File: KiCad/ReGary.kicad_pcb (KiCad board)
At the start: 4 copper layers, 38 x 38 mm, 36 parts, among them U1 10M02SCU169C8G, U2 LM1117-3.3, U3 SN74CBTD16210, U4 SN74CBTD16210, U5 SN74CBTD16210, U6 SN74CBTD16210, U7 PLCC_84_plug, U8 PLCC_84_plug

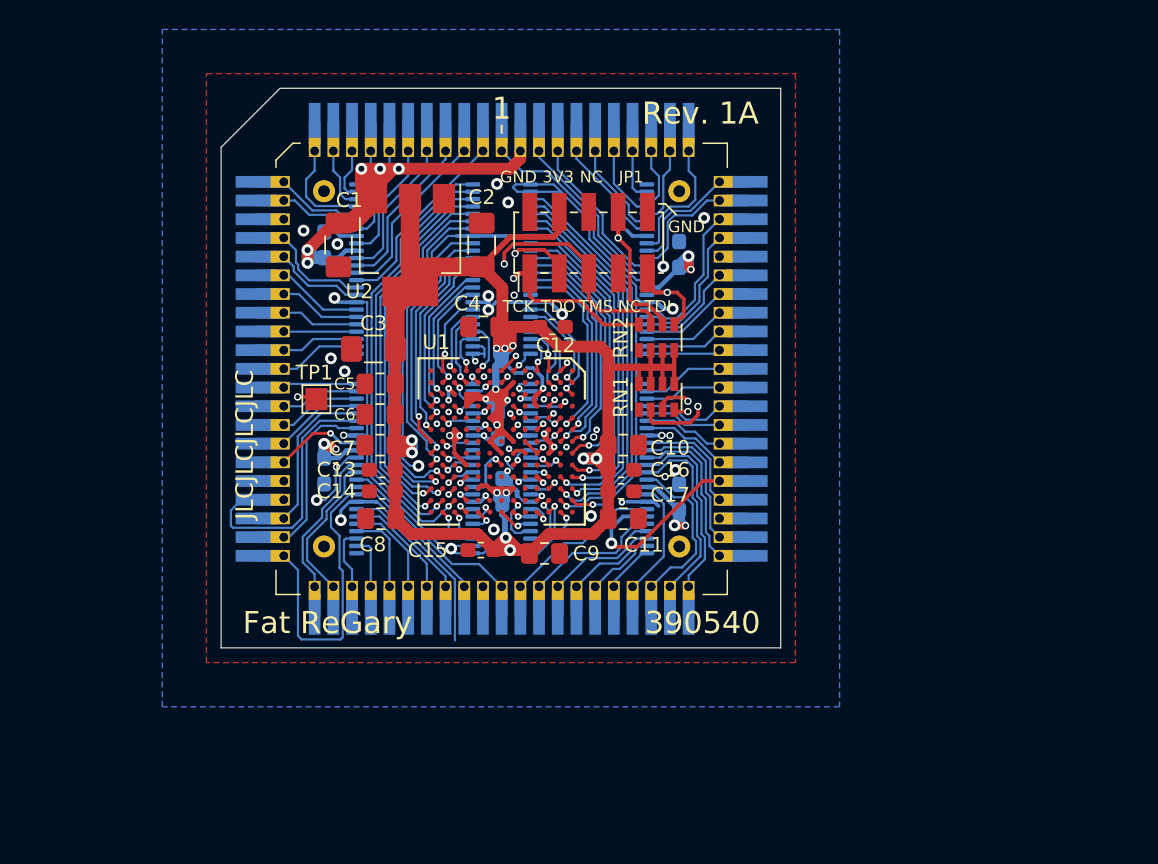
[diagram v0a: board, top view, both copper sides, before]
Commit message: Add Fat Gary socket symbol and change to it
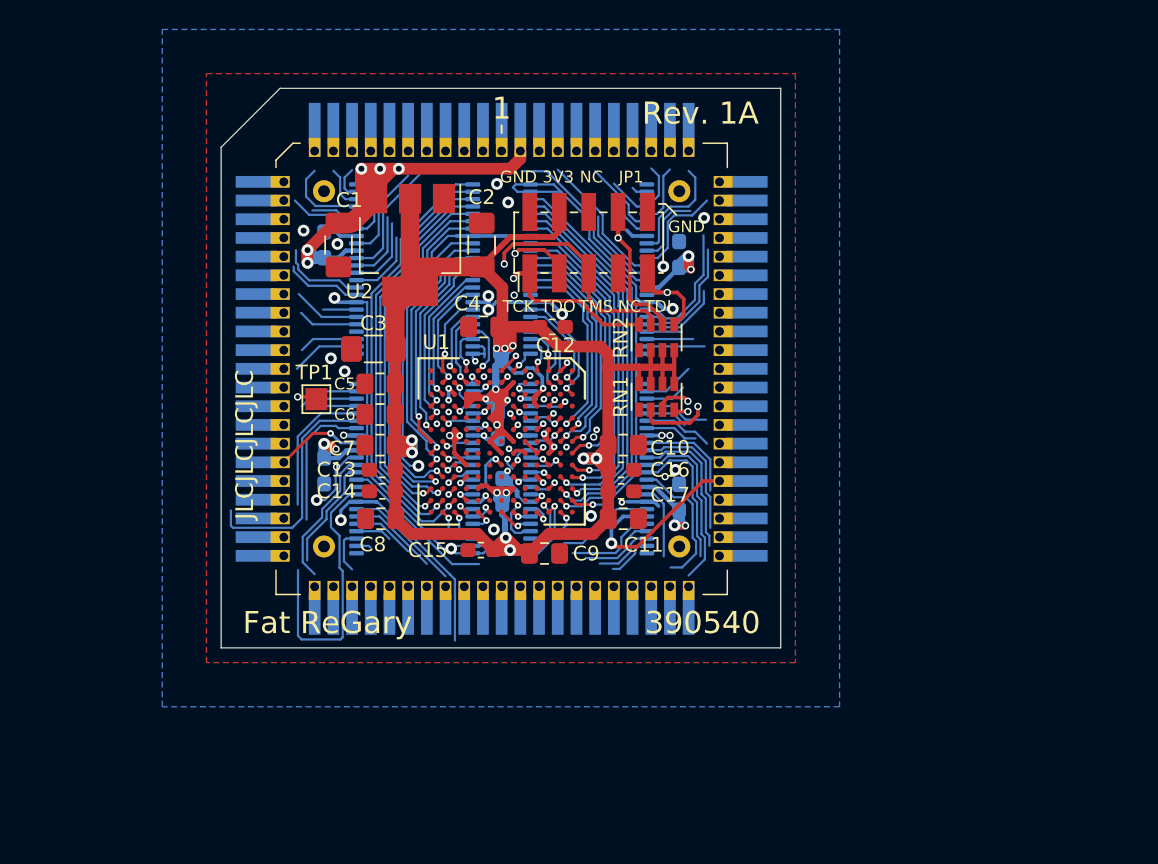
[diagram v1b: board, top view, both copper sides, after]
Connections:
- U7 pad 1: FCS -> Net-(U7-Pad1)
- U7 pad 10: DS -> Net-(U7-Pad10)
- U7 pad 11: DSACK0 -> Net-(U7-Pad11)
- U7 pad 12: DSACK1 -> Net-(U7-Pad12)
- U7 pad 13: STERM -> Net-(U7-Pad13)
- U7 pad 14: GND -> Net-(U7-Pad14)
- U7 pad 15: RMC -> Net-(U7-Pad15)
- U7 pad 16: SBR -> Net-(U7-Pad16)
- U7 pad 17: SBG -> Net-(U7-Pad17)
- U7 pad 18: CIIN -> Net-(U7-Pad18)
- U7 pad 19: MTACK -> Net-(U7-Pad19)
- U7 pad 2: CCS -> Net-(U7-Pad2)
- U7 pad 20: DTACK -> Net-(U7-Pad20)
- U7 pad 21: DOE -> Net-(U7-Pad21)
- U7 pad 22: WAIT -> Net-(U7-Pad22)
- U7 pad 23: BR -> Net-(U7-Pad23)
- U7 pad 24: BG -> Net-(U7-Pad24)
- U7 pad 25: BGACK -> Net-(U7-Pad25)
- U7 pad 26: HLT -> Net-(U7-Pad26)
- U7 pad 27: BERR -> Net-(U7-Pad27)
- U7 pad 28: GND -> Net-(U7-Pad28)
- U7 pad 29: RESET -> Net-(U7-Pad29)
- U7 pad 3: A2 -> Net-(U7-Pad3)
- U7 pad 30: CPUCLK -> Net-(U7-Pad30)
- U7 pad 31: C7M -> Net-(U7-Pad31)
- U7 pad 32: CDAC -> Net-(U7-Pad32)
- U7 pad 33: D2P -> Net-(U7-Pad33)
- U7 pad 34: DBOE1 -> Net-(U7-Pad34)
- U7 pad 35: DBOE0 -> Net-(U7-Pad35)
- U7 pad 36: DBR16 -> Net-(U7-Pad36)
- U7 pad 37: DBLT -> Net-(U7-Pad37)
- U7 pad 38: READ -> Net-(U7-Pad38)
- U7 pad 39: EDS2 -> Net-(U7-Pad39)
- U7 pad 4: A1 -> Net-(U7-Pad4)
- U7 pad 40: EDS3 -> Net-(U7-Pad40)
- U7 pad 41: LOCK_EA1 -> Net-(U7-Pad41)
- U7 pad 42: VCC -> Net-(U7-Pad42)
- U7 pad 43: ABOE2 -> Net-(U7-Pad43)
- U7 pad 44: ABOE0 -> Net-(U7-Pad44)
- U7 pad 45: MS2 -> Net-(U7-Pad45)
- U7 pad 46: MTCR -> Net-(U7-Pad46)
- U7 pad 47: CINH -> Net-(U7-Pad47)
- U7 pad 48: A3 -> Net-(U7-Pad48)
- U7 pad 49: CBREQ -> Net-(U7-Pad49)
- U7 pad 5: A0 -> Net-(U7-Pad5)
- U7 pad 50: CBACK -> Net-(U7-Pad50)
- U7 pad 51: IOZ2 -> Net-(U7-Pad51)
- U7 pad 52: MEMZ2 -> Net-(U7-Pad52)
- U7 pad 53: ADDRZ3 -> Net-(U7-Pad53)
- U7 pad 54: MS1 -> Net-(U7-Pad54)
- U7 pad 55: OWN -> Net-(U7-Pad55)
- U7 pad 56: GND -> Net-(U7-Pad56)
- U7 pad 57: EBGACK -> Net-(U7-Pad57)
- U7 pad 58: CLK90 -> Net-(U7-Pad58)
- U7 pad 59: SLAVE4 -> Net-(U7-Pad59)
- U7 pad 6: RW -> Net-(U7-Pad6)
- U7 pad 60: EA2 -> Net-(U7-Pad60)
- U7 pad 61: EA3 -> Net-(U7-Pad61)
- U7 pad 62: EDS0 -> Net-(U7-Pad62)
- U7 pad 63: EBCLR -> Net-(U7-Pad63)
- U7 pad 64: SLAVE3 -> Net-(U7-Pad64)
- U7 pad 65: SLAVE2 -> Net-(U7-Pad65)
- U7 pad 66: SLAVE1 -> Net-(U7-Pad66)
- U7 pad 67: SLAVE0 -> Net-(U7-Pad67)
- U7 pad 68: BIGZ -> Net-(U7-Pad68)
- U7 pad 69: EBG4 -> Net-(U7-Pad69)
- U7 pad 7: SIZ0 -> Net-(U7-Pad7)
- U7 pad 70: GND -> Net-(U7-Pad70)
- U7 pad 71: EBG3 -> Net-(U7-Pad71)
- U7 pad 72: EBG2 -> Net-(U7-Pad72)
- U7 pad 73: EBG1 -> Net-(U7-Pad73)
- U7 pad 74: EBG0 -> Net-(U7-Pad74)
- U7 pad 75: ABOE1 -> Net-(U7-Pad75)
- U7 pad 76: EBR4 -> Net-(U7-Pad76)
- U7 pad 77: EBR3 -> Net-(U7-Pad77)
- U7 pad 78: EBR2 -> Net-(U7-Pad78)
- U7 pad 79: EBR1 -> Net-(U7-Pad79)
- U7 pad 8: SIZ1 -> Net-(U7-Pad8)
- U7 pad 80: EBR0 -> Net-(U7-Pad80)
- U7 pad 81: MS0 -> Net-(U7-Pad81)
- U7 pad 82: BINT -> Net-(U7-Pad82)
- U7 pad 83: EDS1 -> Net-(U7-Pad83)
- U7 pad 84: VCC -> Net-(U7-Pad84)
- U7 pad 9: AS -> Net-(U7-Pad9)
- U8 pad 1: FCS -> Net-(U8-Pad1)
- U8 pad 10: DS -> Net-(U8-Pad10)
- U8 pad 11: DSACK0 -> Net-(U8-Pad11)
- U8 pad 12: DSACK1 -> Net-(U8-Pad12)
- U8 pad 13: STERM -> Net-(U8-Pad13)
- U8 pad 14: GND -> Net-(U8-Pad14)
- U8 pad 15: RMC -> Net-(U8-Pad15)
- U8 pad 16: SBR -> Net-(U8-Pad16)
- U8 pad 17: SBG -> Net-(U8-Pad17)
- U8 pad 18: CIIN -> Net-(U8-Pad18)
- U8 pad 19: MTACK -> Net-(U8-Pad19)
- U8 pad 2: CCS -> Net-(U8-Pad2)
- U8 pad 20: DTACK -> Net-(U8-Pad20)
- U8 pad 21: DOE -> Net-(U8-Pad21)
- U8 pad 22: WAIT -> Net-(U8-Pad22)
- U8 pad 23: BR -> Net-(U8-Pad23)
- U8 pad 24: BG -> Net-(U8-Pad24)
- U8 pad 25: BGACK -> Net-(U8-Pad25)
- U8 pad 26: HLT -> Net-(U8-Pad26)
- U8 pad 27: BERR -> Net-(U8-Pad27)
- U8 pad 28: GND -> Net-(U8-Pad28)
- U8 pad 29: RESET -> Net-(U8-Pad29)
- U8 pad 3: A2 -> Net-(U8-Pad3)
- U8 pad 30: CPUCLK -> Net-(U8-Pad30)
- U8 pad 31: C7M -> Net-(U8-Pad31)
- U8 pad 32: CDAC -> Net-(U8-Pad32)
- U8 pad 33: D2P -> Net-(U8-Pad33)
- U8 pad 34: DBOE1 -> Net-(U8-Pad34)
- U8 pad 35: DBOE0 -> Net-(U8-Pad35)
- U8 pad 36: DBR16 -> Net-(U8-Pad36)
- U8 pad 37: DBLT -> Net-(U8-Pad37)
- U8 pad 38: READ -> Net-(U8-Pad38)
- U8 pad 39: EDS2 -> Net-(U8-Pad39)
- U8 pad 4: A1 -> Net-(U8-Pad4)
- U8 pad 40: EDS3 -> Net-(U8-Pad40)
- U8 pad 41: LOCK_EA1 -> Net-(U8-Pad41)
- U8 pad 42: VCC -> Net-(U8-Pad42)
- U8 pad 43: ABOE2 -> Net-(U8-Pad43)
- U8 pad 44: ABOE0 -> Net-(U8-Pad44)
- U8 pad 45: MS2 -> Net-(U8-Pad45)
- U8 pad 46: MTCR -> Net-(U8-Pad46)
- U8 pad 47: CINH -> Net-(U8-Pad47)
- U8 pad 48: A3 -> Net-(U8-Pad48)
- U8 pad 49: CBREQ -> Net-(U8-Pad49)
- U8 pad 5: A0 -> Net-(U8-Pad5)
- U8 pad 50: CBACK -> Net-(U8-Pad50)
- U8 pad 51: IOZ2 -> Net-(U8-Pad51)
- U8 pad 52: MEMZ2 -> Net-(U8-Pad52)
- U8 pad 53: ADDRZ3 -> Net-(U8-Pad53)
- U8 pad 54: MS1 -> Net-(U8-Pad54)
- U8 pad 55: OWN -> Net-(U8-Pad55)
- U8 pad 56: GND -> Net-(U8-Pad56)
- U8 pad 57: EBGACK -> Net-(U8-Pad57)
- U8 pad 58: CLK90 -> Net-(U8-Pad58)
- U8 pad 59: SLAVE4 -> Net-(U8-Pad59)
- U8 pad 6: RW -> Net-(U8-Pad6)
- U8 pad 60: EA2 -> Net-(U8-Pad60)
- U8 pad 61: EA3 -> Net-(U8-Pad61)
- U8 pad 62: EDS0 -> Net-(U8-Pad62)
- U8 pad 63: EBCLR -> Net-(U8-Pad63)
- U8 pad 64: SLAVE3 -> Net-(U8-Pad64)
- U8 pad 65: SLAVE2 -> Net-(U8-Pad65)
- U8 pad 66: SLAVE1 -> Net-(U8-Pad66)
- U8 pad 67: SLAVE0 -> Net-(U8-Pad67)
- U8 pad 68: BIGZ -> Net-(U8-Pad68)
- U8 pad 69: EBG4 -> Net-(U8-Pad69)
- U8 pad 7: SIZ0 -> Net-(U8-Pad7)
- U8 pad 70: GND -> Net-(U8-Pad70)
- U8 pad 71: EBG3 -> Net-(U8-Pad71)
- U8 pad 72: EBG2 -> Net-(U8-Pad72)
- U8 pad 73: EBG1 -> Net-(U8-Pad73)
- U8 pad 74: EBG0 -> Net-(U8-Pad74)
- U8 pad 75: ABOE1 -> Net-(U8-Pad75)
- U8 pad 76: EBR4 -> Net-(U8-Pad76)
- U8 pad 77: EBR3 -> Net-(U8-Pad77)
- U8 pad 78: EBR2 -> Net-(U8-Pad78)
- U8 pad 79: EBR1 -> Net-(U8-Pad79)
- U8 pad 8: SIZ1 -> Net-(U8-Pad8)
- U8 pad 80: EBR0 -> Net-(U8-Pad80)
- U8 pad 81: MS0 -> Net-(U8-Pad81)
- U8 pad 82: BINT -> Net-(U8-Pad82)
- U8 pad 83: EDS1 -> Net-(U8-Pad83)
- U8 pad 84: VCC -> Net-(U8-Pad84)
- U8 pad 9: AS -> Net-(U8-Pad9)
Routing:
- net LOCK_EA1: track 12.2 -> 0.84 mm
- net CCS: track 15.0 -> 4.84 mm
- net A2: track 13.9 -> 5.13 mm
- net A1: track 12.8 -> 4.84 mm
- net EDS1: track 13.6 -> 5.64 mm
- net GND: track 133.1 -> 125.7 mm
- net MS0: track 9.51 -> 2.53 mm
- net SLAVE2: track 6.90 -> 0.00 mm
- net BR: track 6.90 -> 0.00 mm
- net DTACK: track 6.81 -> 0.00 mm
- net ABOE0: track 12.6 -> 6.59 mm
- net SBG: track 7.77 -> 2.27 mm
- net HLT: track 7.86 -> 2.38 mm
- net BIGZ: track 7.86 -> 2.38 mm
- net CBREQ: track 5.24 -> 0.00 mm
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
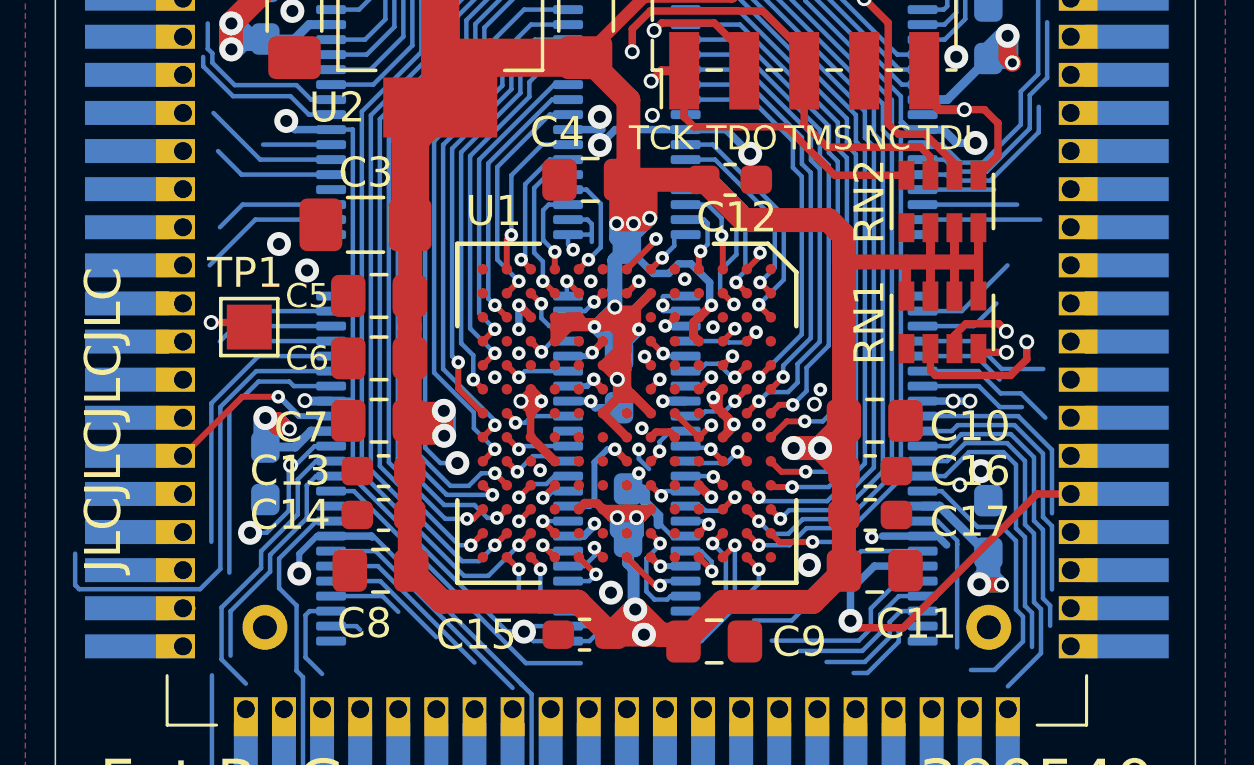
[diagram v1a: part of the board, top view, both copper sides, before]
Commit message: Removed BGA FPGA
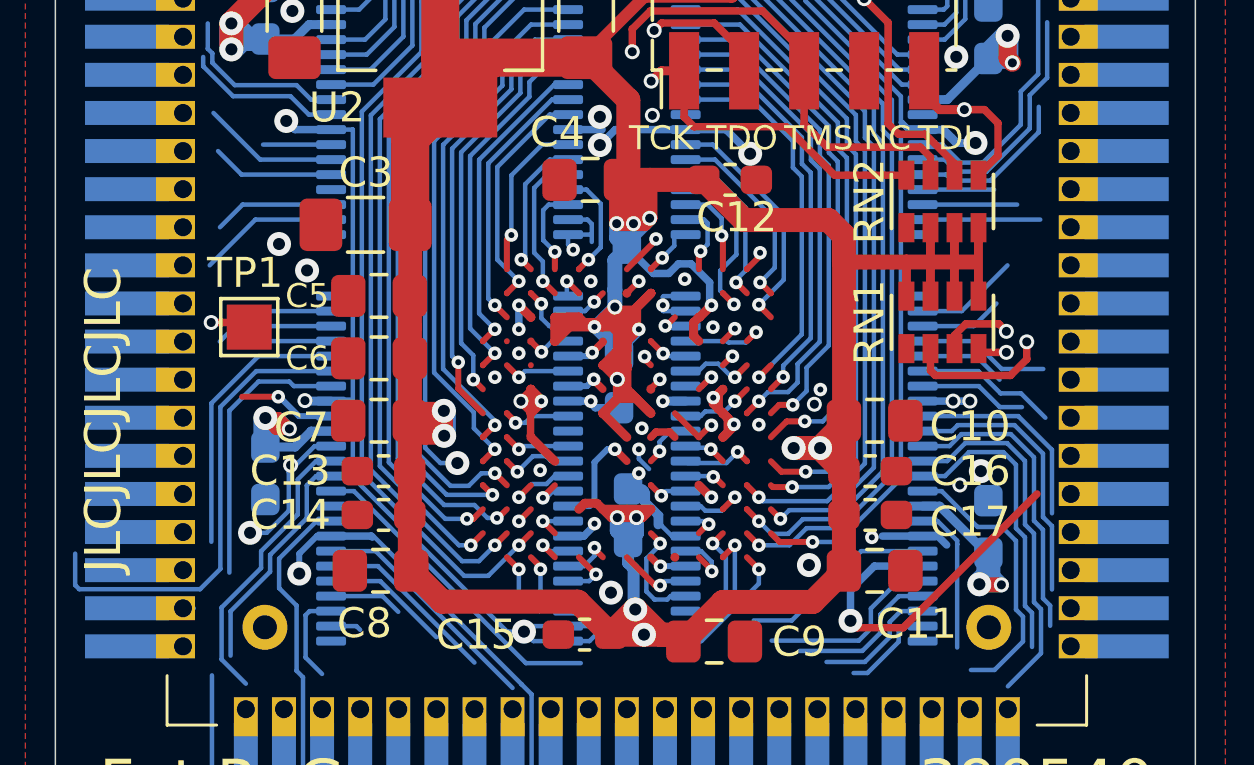
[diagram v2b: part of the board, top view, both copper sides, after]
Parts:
- removed U1: 10M02SCU169C8G, ReGary:BGA-169_11.0x11.0mm_Layout13x13_P0.8mm_Ball0.5mm_Pad0.35mm_NSMD
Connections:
- TP1 pad 1: TP1 -> Net-(TP1-Pad1)
- U7 pad 1: Net-(U7-Pad1) -> GND
- U7 pad 17: Net-(U7-Pad17) -> GND
- U7 pad 34: Net-(U7-Pad34) -> GND
- U7 pad 42: Net-(U7-Pad42) -> VCC
- U7 pad 51: Net-(U7-Pad51) -> GND
- U7 pad 84: Net-(U7-Pad84) -> VCC
- U8 pad 1: Net-(U8-Pad1) -> GND
- U8 pad 17: Net-(U8-Pad17) -> GND
- U8 pad 34: Net-(U8-Pad34) -> GND
- U8 pad 42: Net-(U8-Pad42) -> VCC
- U8 pad 51: Net-(U8-Pad51) -> GND
- U8 pad 84: Net-(U8-Pad84) -> VCC
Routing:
- net TP1: track 17.1 -> 0.00 mm, vias 2 -> 0
- net Net-(TP1-Pad1): track 0.00 -> 17.1 mm, vias 0 -> 2
- net BERR: track 6.02 -> 3.23 mm
- net CLK90: track 13.0 -> 11.9 mm

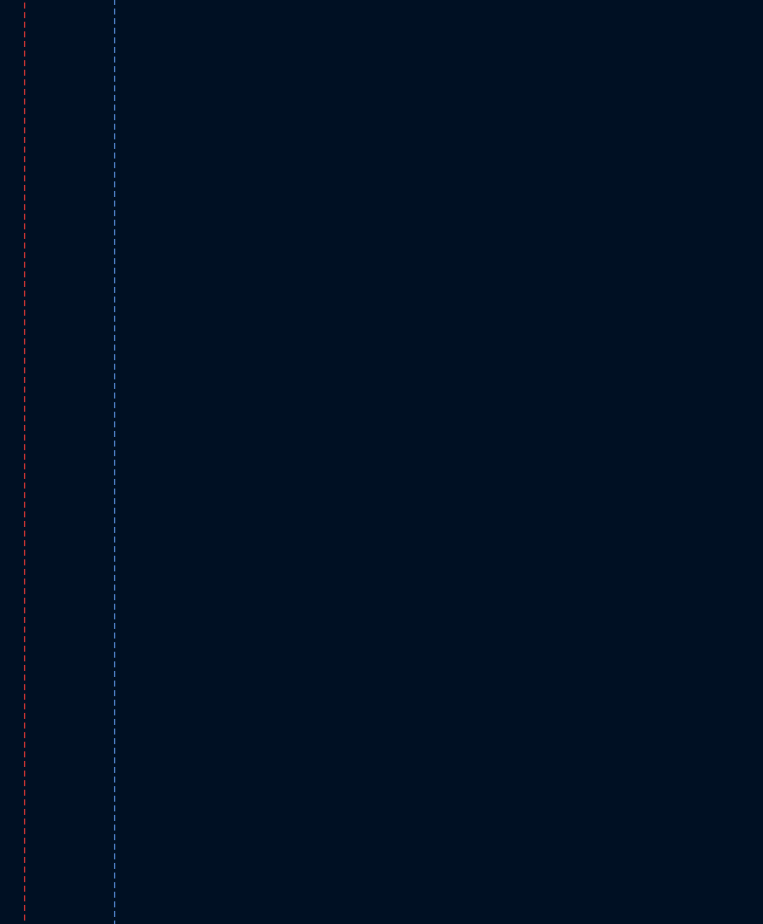
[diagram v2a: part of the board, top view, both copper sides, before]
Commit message: Add Gowin FPGA GW1N-UV1P5LQ100 into the design
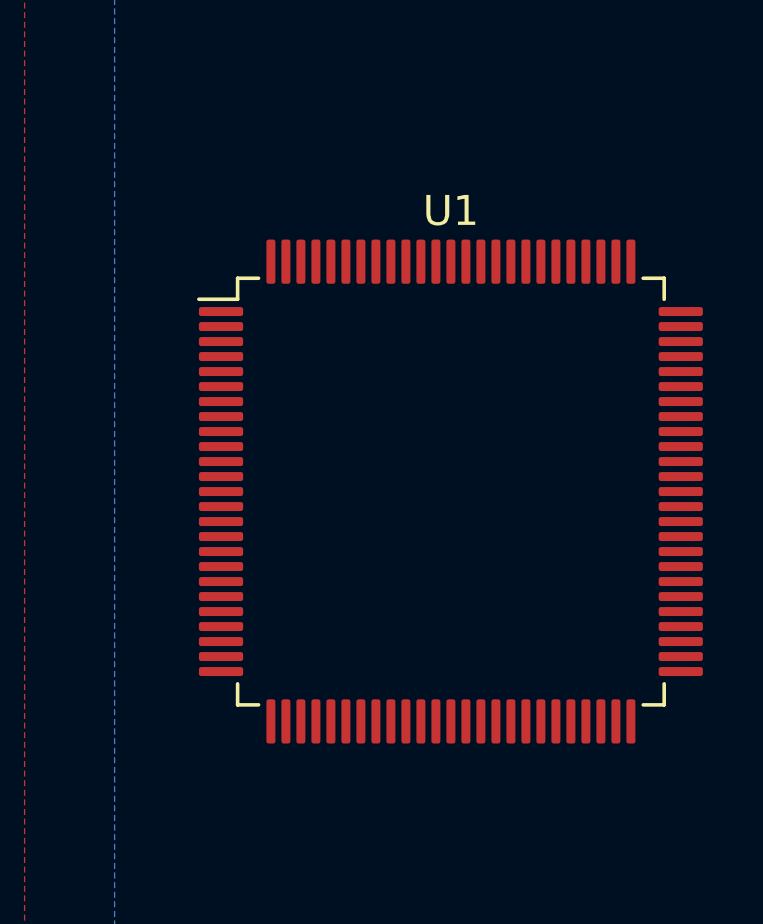
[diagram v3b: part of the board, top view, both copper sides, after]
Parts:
- added U1: GW1N-UV1P5LQ100, Package_QFP:TQFP-100_14x14mm_P0.5mm, F.Cu at (178.6, 80.0)

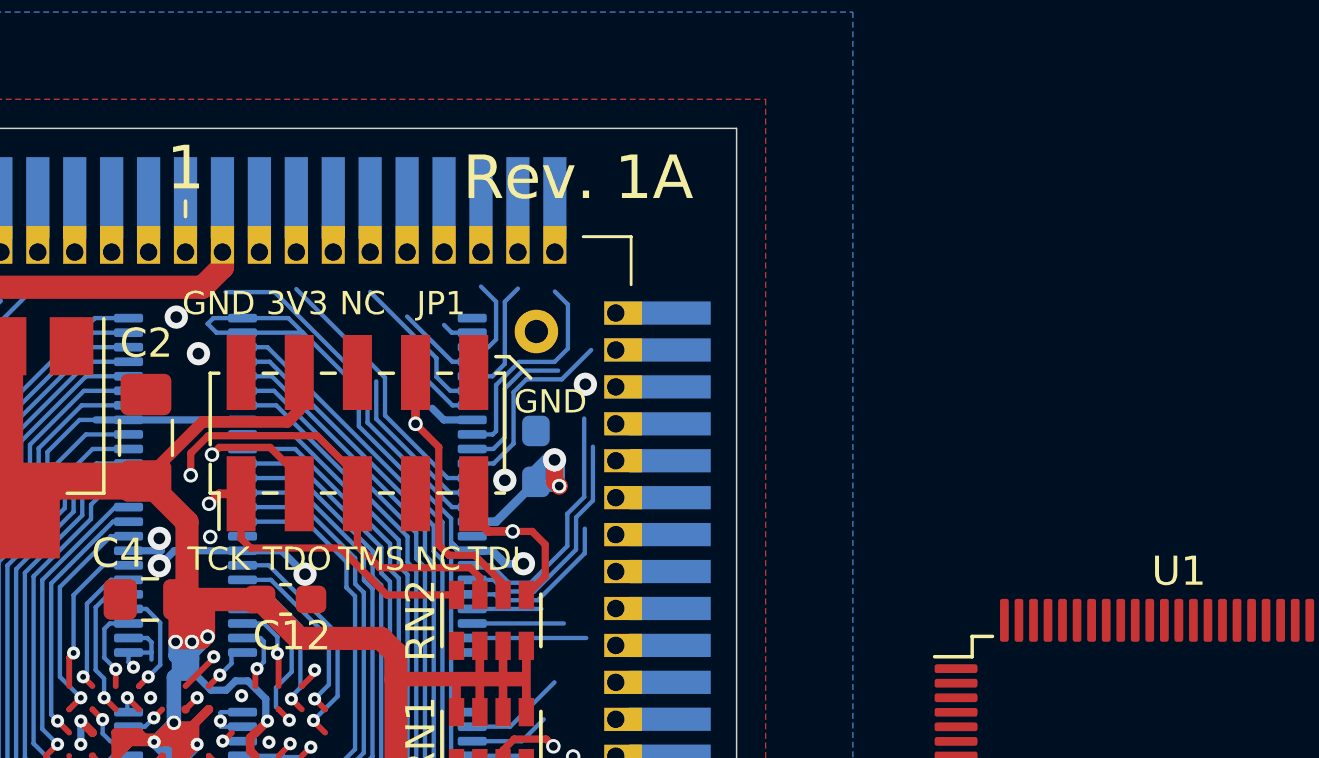
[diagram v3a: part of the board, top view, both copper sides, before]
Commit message: Change to 6-pin JTAG-header
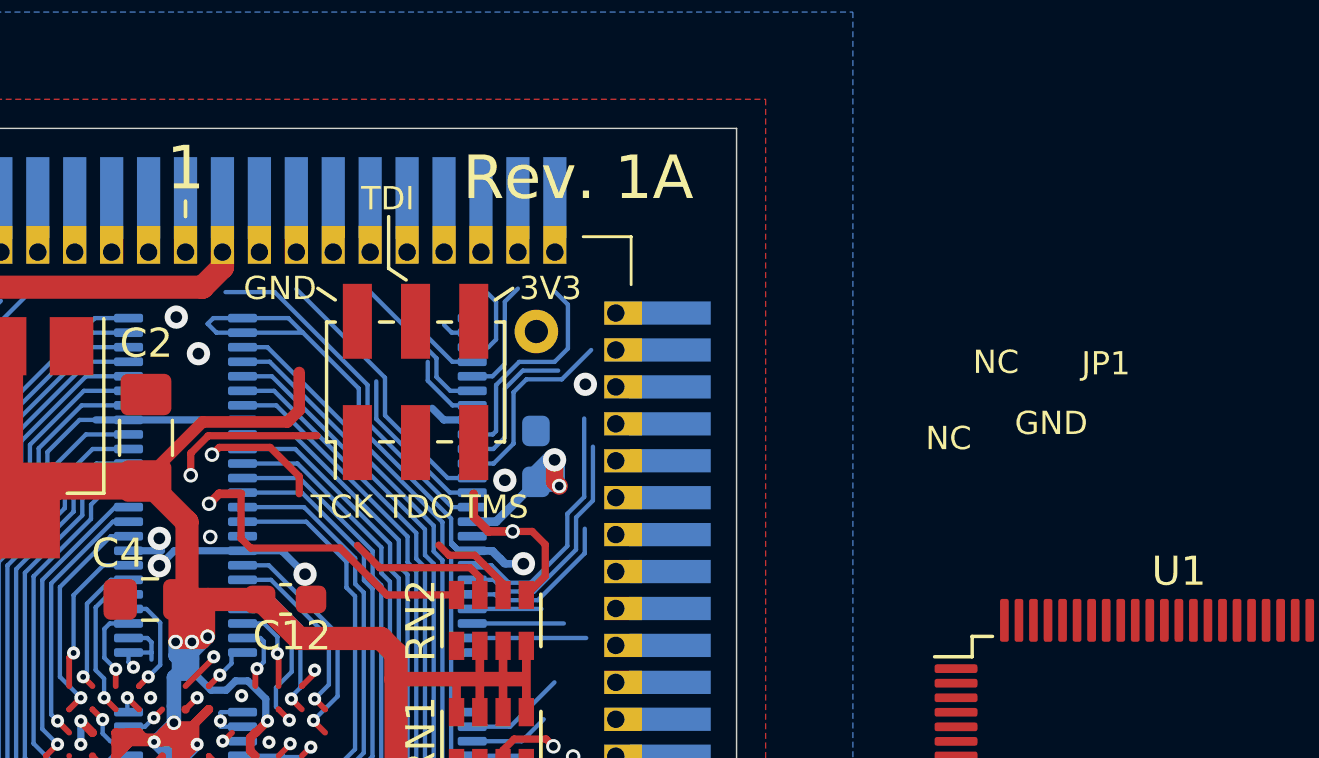
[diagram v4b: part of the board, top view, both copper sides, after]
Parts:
- JTAG1: value Conn_02x05_Odd_Even -> Conn_02x03_Odd_Even; footprint Connector_PinHeader_2.00mm:PinHeader_2x05_P2.00mm_Vertical_SMD -> Connector_PinHeader_2.00mm:PinHeader_2x03_P2.00mm_Vertical_SMD
- moved JTAG1 2.66 mm to (152.4, 64.1)
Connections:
- JTAG1 pad 4: 3V3 -> TDI
- JTAG1 pad 6: Net-(JTAG1-Pad6) -> 3V3
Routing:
- net JP1: track 21.1 -> 13.8 mm, vias 2 -> 1
- net TMS: track 23.3 -> 18.9 mm
